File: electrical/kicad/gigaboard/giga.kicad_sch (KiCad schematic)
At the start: 47 parts, among them J1 Conn_02x03_Counter_Clockwise, J10 Conn_01x04, J11 Conn_01x04, J12 Conn_01x04, J13 Conn_01x06, J14 Conn_01x18, J15 Conn_01x04, J16 Conn_01x12, J17 Conn_01x04, J18 Conn_01x12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

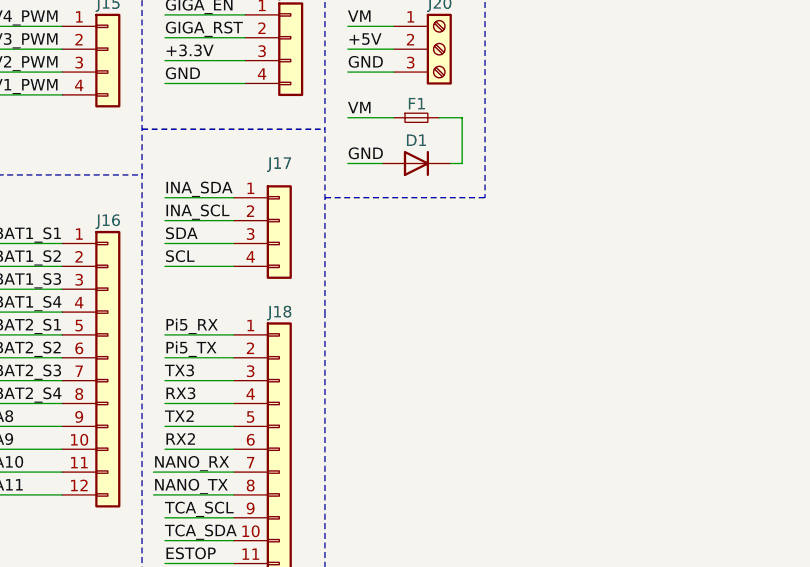
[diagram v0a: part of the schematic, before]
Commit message: add(kicad/rev): schematics and PCB images for previous designs
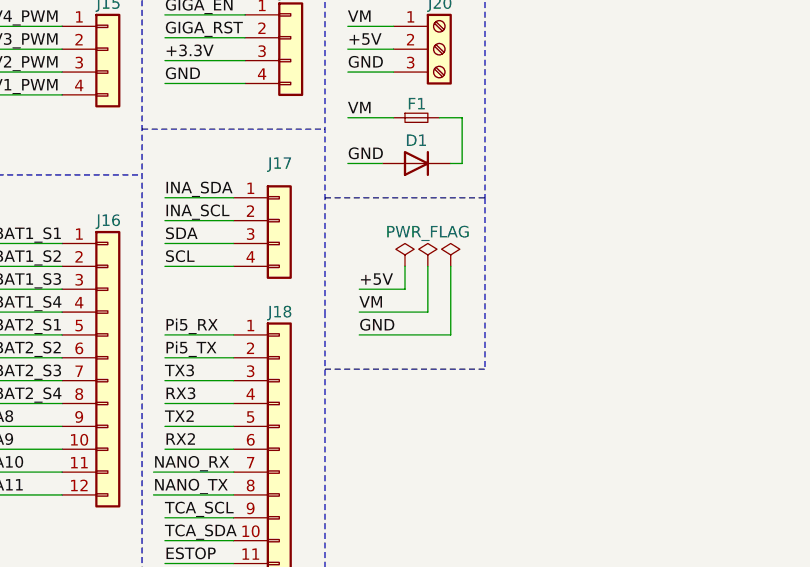
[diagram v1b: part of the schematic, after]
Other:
- title: Giga Board -> GigaBoard
